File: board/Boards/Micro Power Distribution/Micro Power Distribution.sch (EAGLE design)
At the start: 24 parts

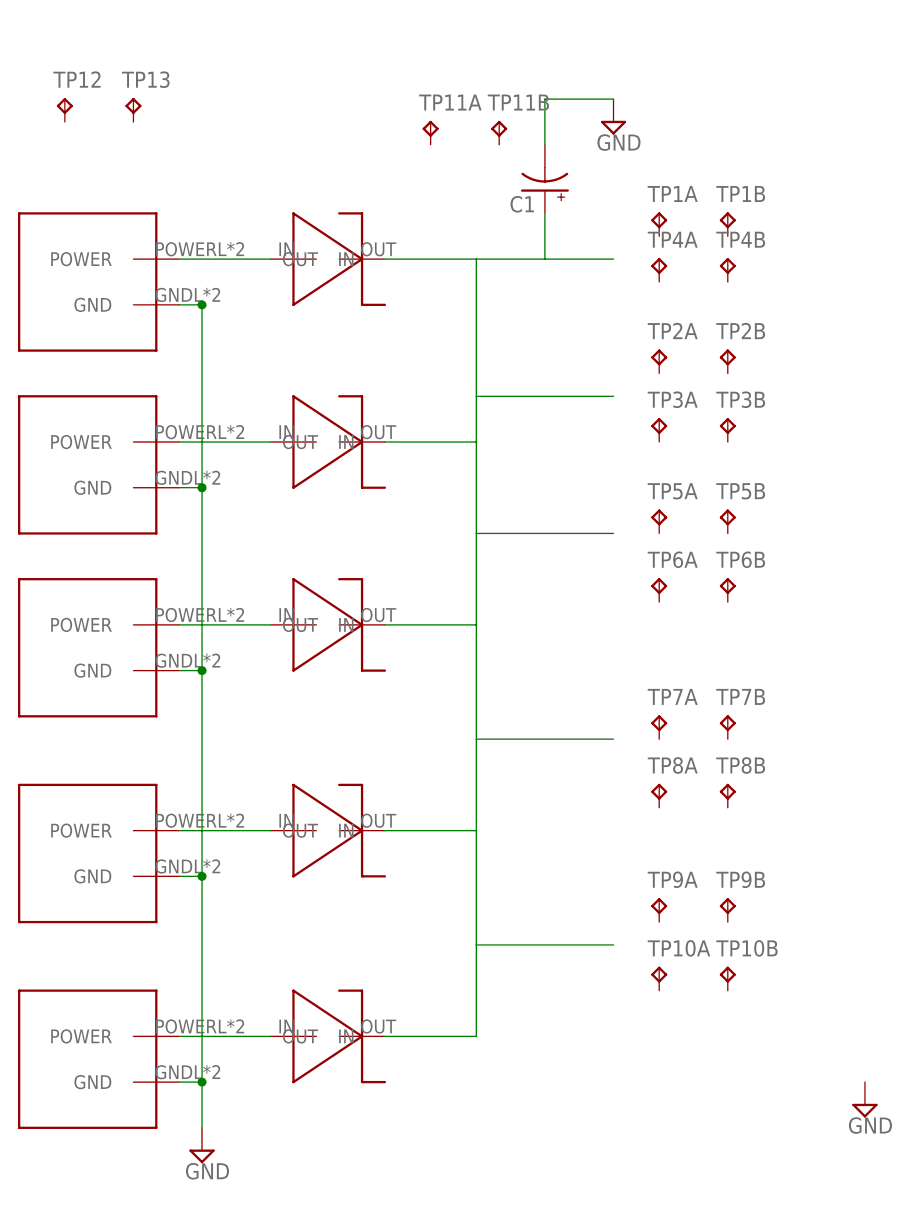
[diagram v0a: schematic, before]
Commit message: updated power dist. board + created a micro version
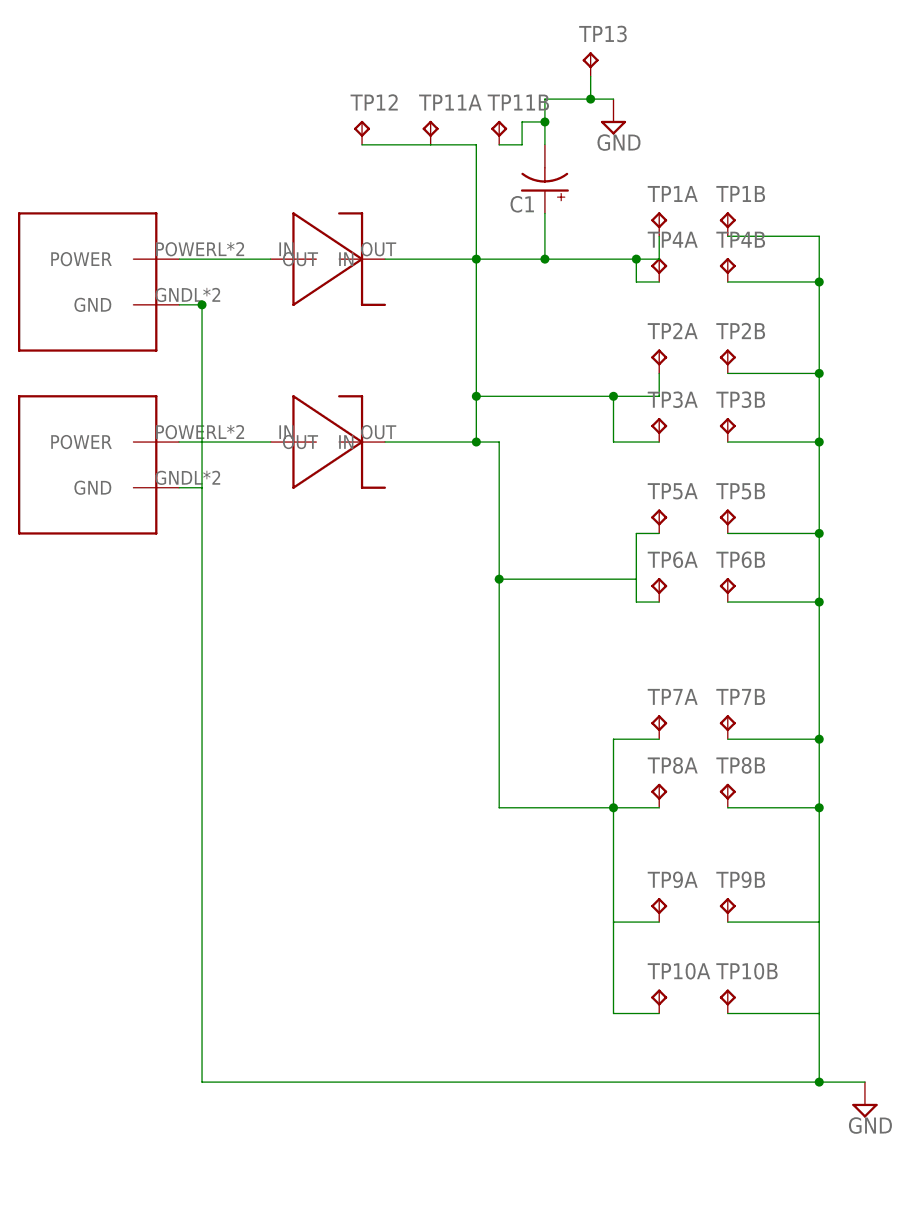
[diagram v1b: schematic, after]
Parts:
- removed U$10, U$8, U$9: DO-214AB, Diodes:DO-214AB
- removed U$2, U$3, U$4: 2X2-MOLEX, Molex:2X2-MOLEX
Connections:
- removed net N$3: U$2.POWER, U$8.IN
- removed net N$4: U$3.POWER, U$9.IN
- removed net N$5: U$10.IN, U$4.POWER
- removed net N$6: C1.+, U$10.OUT, U$6.OUT, U$7.OUT, U$8.OUT, U$9.OUT
- new net N$10: C1.+, TP10A.TP, TP11A.TP, TP12.TP, TP1A.TP, TP2A.TP, TP3A.TP, TP4A.TP, TP5A.TP, TP6A.TP, TP7A.TP, TP8A.TP, TP9A.TP, U$6.OUT, U$7.OUT
- net GND: now also TP10B.TP, TP11B.TP, TP13.TP, TP1B.TP, TP2B.TP, TP3B.TP, TP4B.TP, TP5B.TP, TP6B.TP, TP7B.TP, TP8B.TP, TP9B.TP; no longer U$2.GND, U$3.GND, U$4.GND
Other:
- moved on the sheet: TP10A, TP10B, TP12, TP13
